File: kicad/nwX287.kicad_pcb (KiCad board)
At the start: 2 copper layers, 52.5 x 24 mm, 4 parts, among them U1 bq3285, U2 Socket, Y1 32.768kHz 6pF

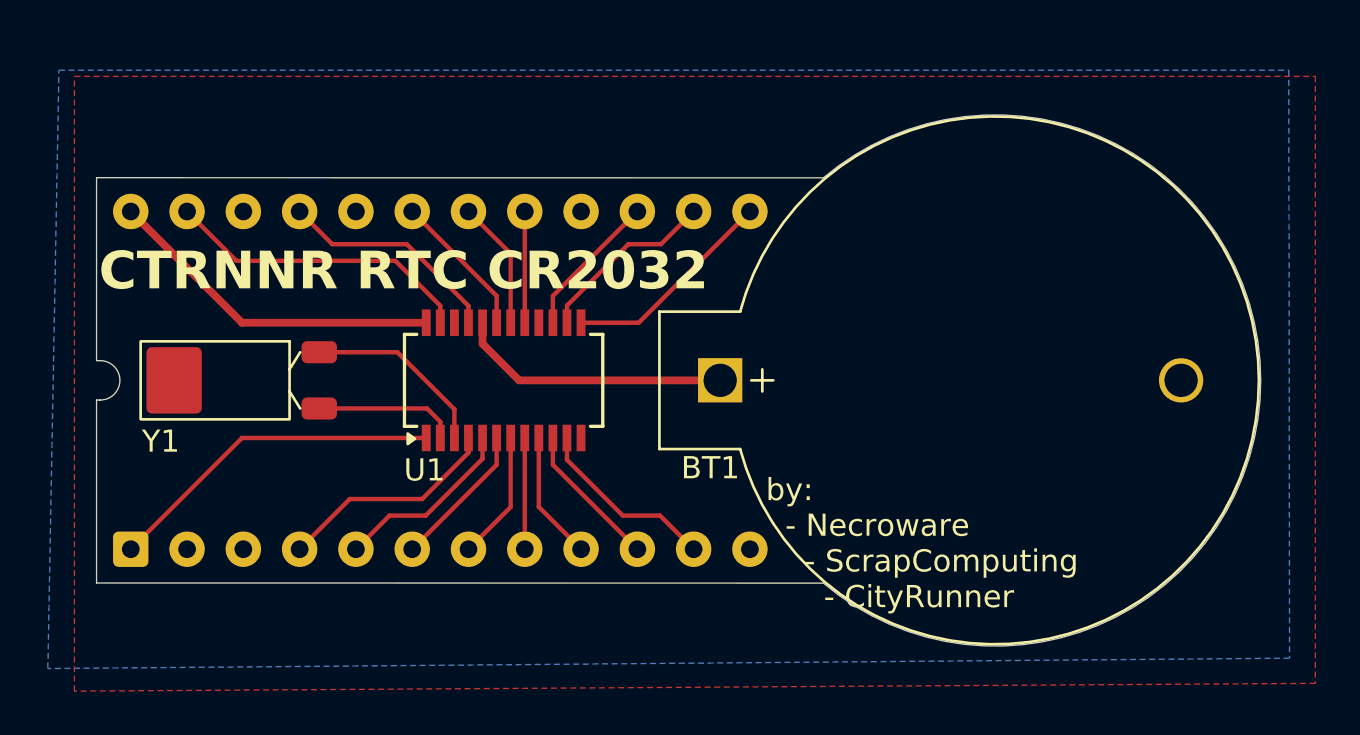
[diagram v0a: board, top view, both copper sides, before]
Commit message: add teardrops
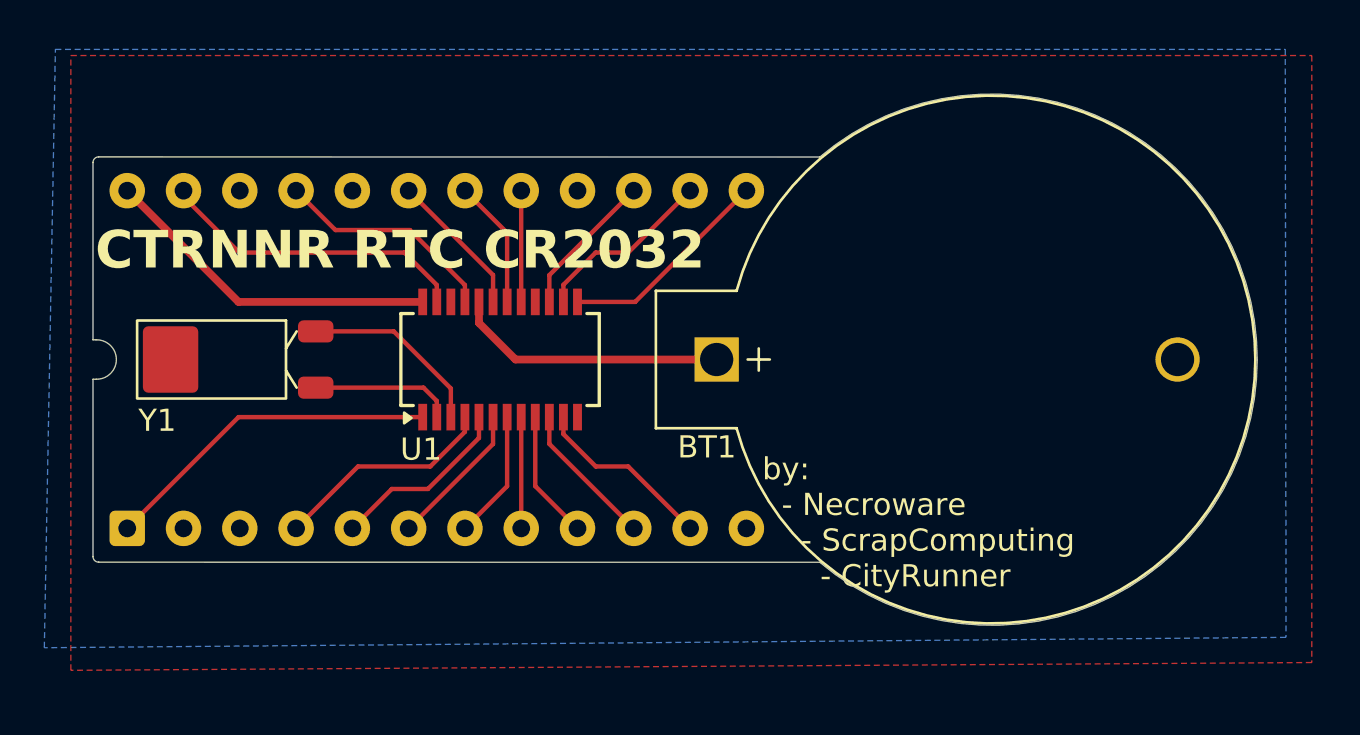
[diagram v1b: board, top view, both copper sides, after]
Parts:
- moved Y1 0.95 mm to (123.6, 108.2)
- moved BT1 0.95 mm to (145.0, 108.2)
- moved U1 0.95 mm to (135.2, 108.2)
- moved U2 0.95 mm to (118.4, 115.8)
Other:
- outline, holes or cut-outs redrawn

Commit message: add stitching vias
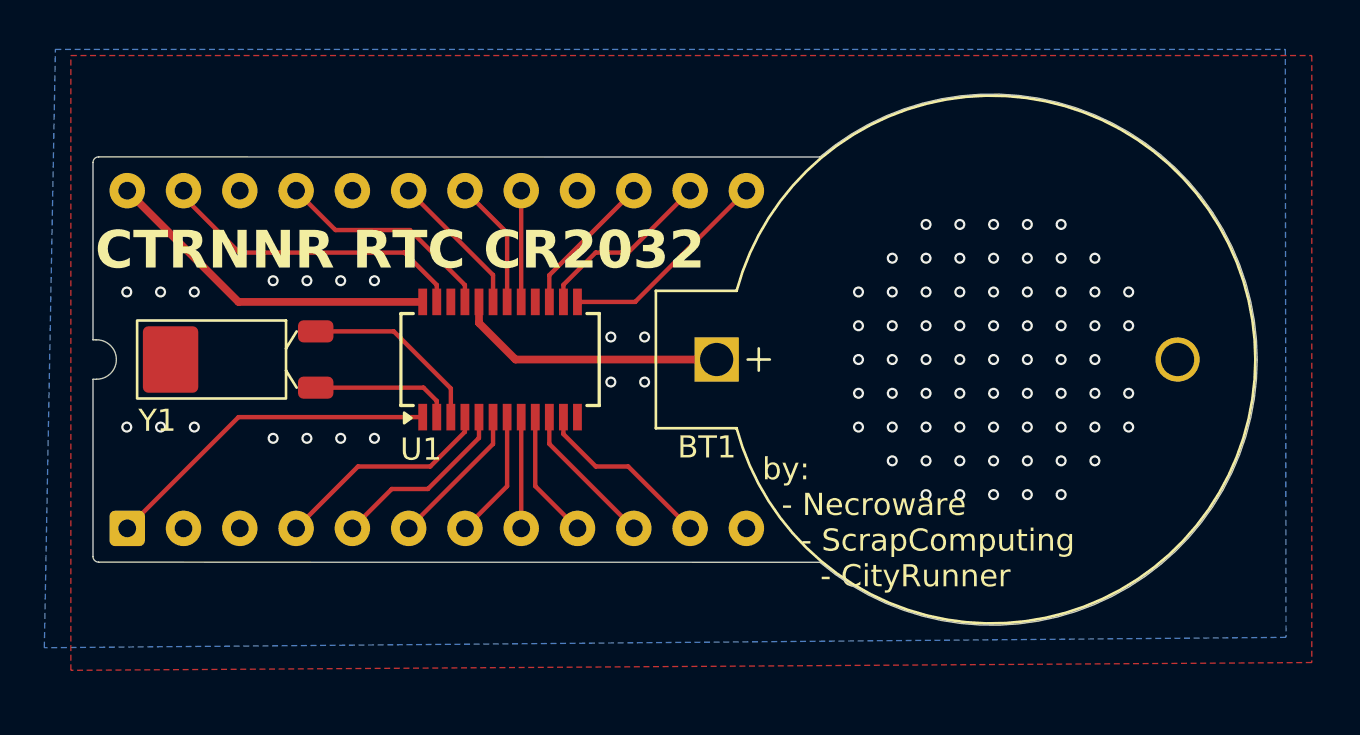
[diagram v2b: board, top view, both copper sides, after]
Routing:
- net GND: vias 0 -> 86
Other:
- board text added: "MOT NC NC AD0 AD1 AD2 AD3 AD4 AD5 AD6 AD7 GND"
- board text added: "VCC SQW NC RCL NC INT RST DS NC R/W AS CS"

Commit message: adjust layout and silkscreen
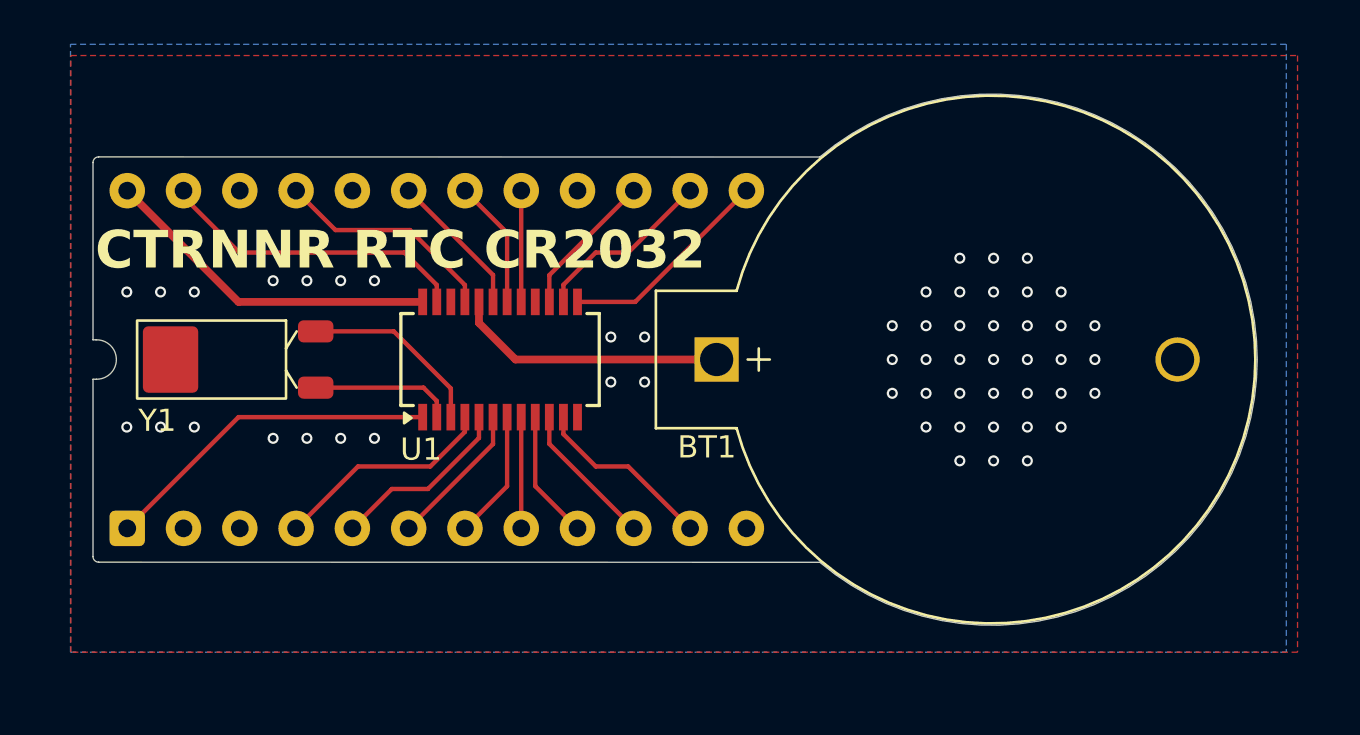
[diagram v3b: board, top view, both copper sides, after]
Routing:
- net GND: vias 86 -> 55
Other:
- board text added: "github.com/CityRunner/rtc-cr2032-ssop"
- board text removed: "by: - Necroware - ScrapComputing - CityRunner"

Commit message: update readme
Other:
- board text added: "CTRNNR INT RTC CR2032"
- board text removed: "CTRNNR RTC CR2032"
